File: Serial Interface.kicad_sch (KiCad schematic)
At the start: 0 parts

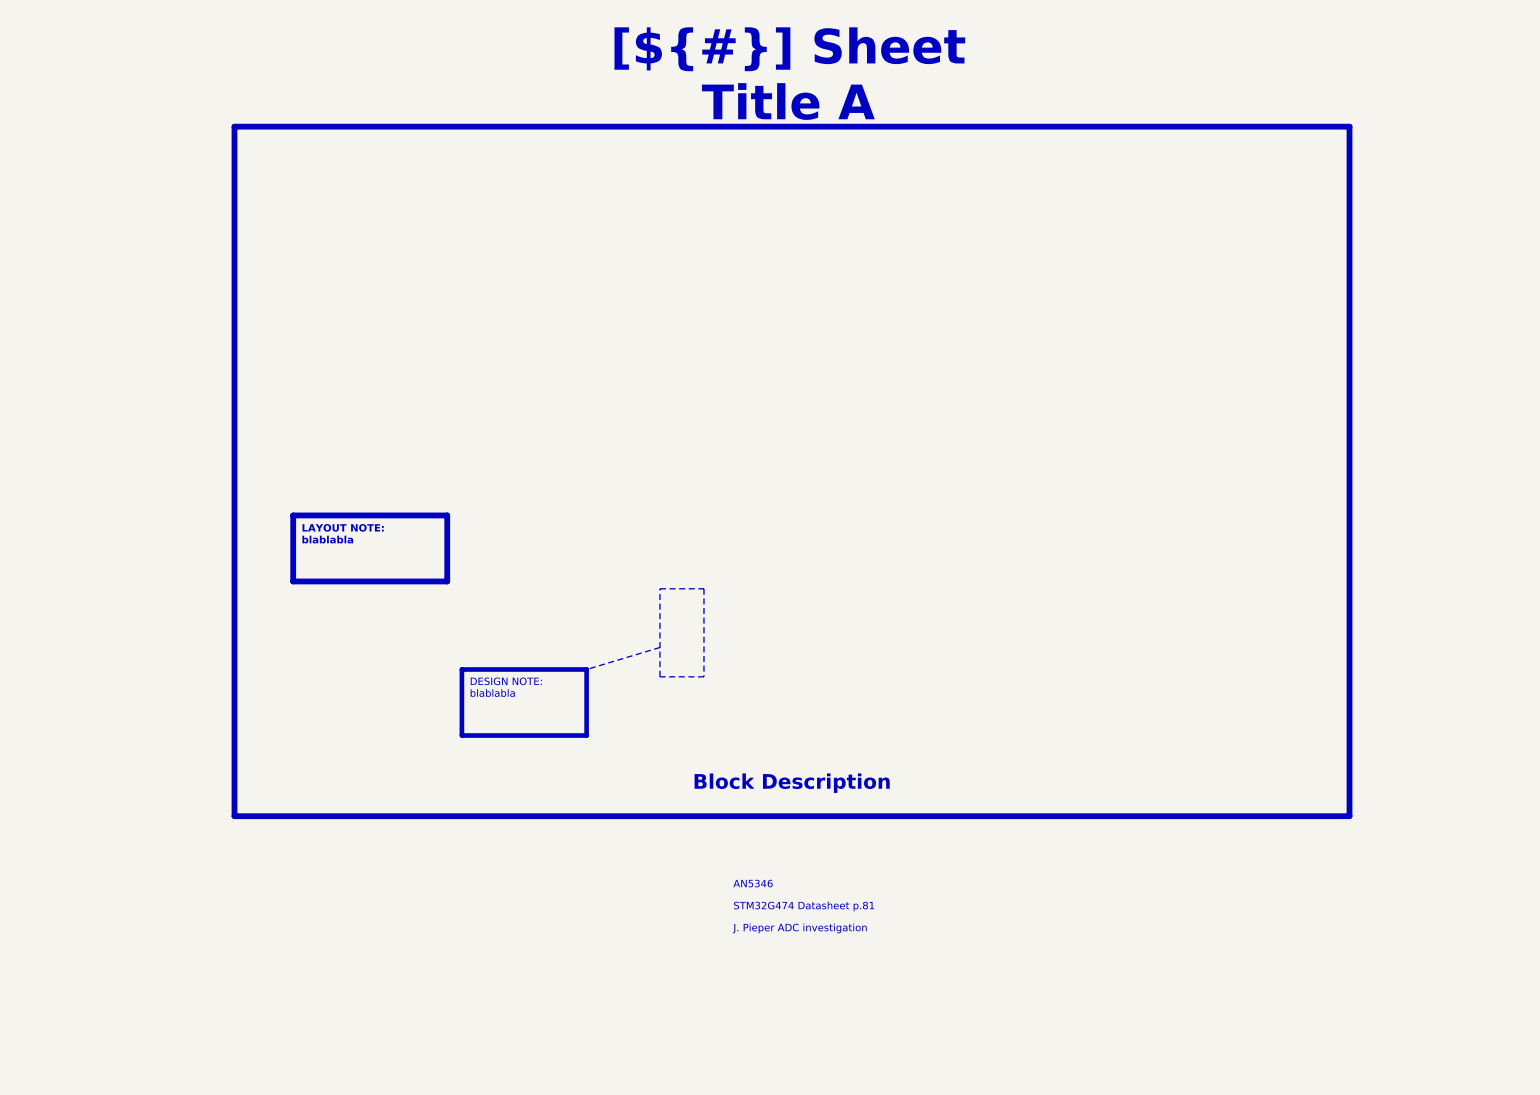
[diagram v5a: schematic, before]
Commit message: [Project][Added] CI/CD environment
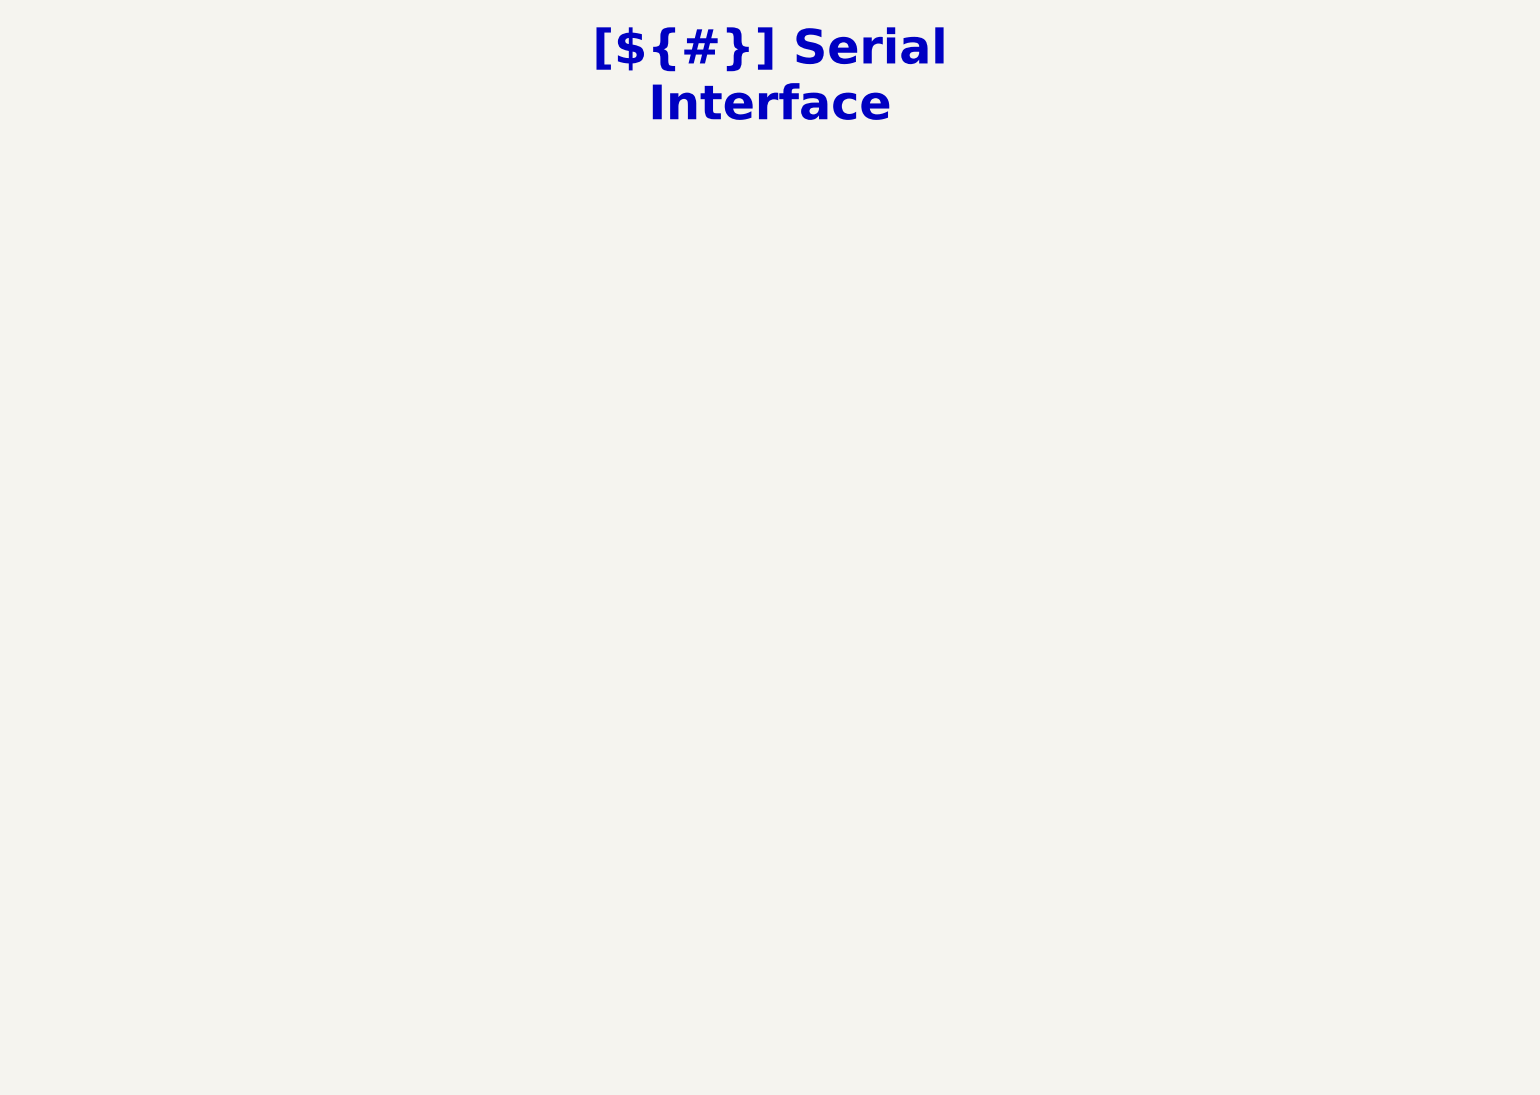
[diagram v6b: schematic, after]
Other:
- note removed: "AN5346"
- note removed: "J. Pieper ADC investigation"
- note removed: "STM32G474 Datasheet p.81"
- title: Sheet Title A -> Serial Interface
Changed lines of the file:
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@@
 (kicad_sch
-	(version 20260306)
+	(version 20250114)
 	(generator "eeschema")
-	(generator_version "10.0")
+	(generator_version "9.0")
 	(paper "A4")
 	(title_block
-		(title "Sheet Title A")
+		(title "Serial Interface")
 		(date "2025-01-12")
 		(rev "${REVISION}")
 		(company "${COMPANY}")
 	)
-	(rectangle
-		(start 129.54 110.49)
-		(end 137.16 125.73)
-		(stroke
-			(width 0)
-			(type dot)
-			(color 255 0 0 1)
-		)
-		(fill
-			(type none)
-		)
-	)
-	(rectangle
-		(start 55.88 30.48)
-		(end 248.92 149.86)
-		(stroke
-			(width 1)
-			(type default)
-			(color 200 200 200 1)
-		)
-		(fill
-			(type none)
-		)
-	)
-	(text "J. Pieper ADC investigation"
-		(exclude_from_sim no)
-		(at 142.24 170.18 0)
-		(effects
-			(font
-				(face "Arial")
-				(size 1.27 1.27)
-				(color 0 0 0 1)
-			)
-			(justify left bottom)
-			(href "https://jpieper.com/2023/07/24/stm32g4-adc-performance-part-2/")
-		)
-	)
-	(text "STM32G474 Datasheet p.81"
-		(exclude_from_sim no)
-		(at 142.24 166.37 0)
-		(effects
-			(font
-				(face "Arial")
-				(size 1.27 1.27)
-				(color 0 0 0 1)
-			)
-			(justify left bottom)
-			(href "https://www.st.com/resource/en/datasheet/stm32g474cb.pdf")
-		)
-	)
-	(text "AN5346"
-		(exclude_from_sim no)
-		(at 142.24 162.56 0)
-		(effects
-			(font
-				(face "Arial")
-				(size 1.27 1.27)
-				(color 0 0 0 1)
-			)
-			(justify left bottom)
-			(href "https://www.st.com/resource/en/application_note/an5346-stm32g4-adc-use-tips-and-recommendations-stmicroelectronics.pdf")
-		)
-	)
-	(text_box "LAYOUT NOTE:\nblablabla"
-		(exclude_from_sim no)
-		(at 66.04 97.79 0)
-		(size 26.67 11.43)
-		(margins 1.4525 1.4525 1.4525 1.4525)
-		(stroke
-			(width 1)
-			(type solid)
-			(color 0 0 255 1)
-		)
-		(fill
-			(type none)
-		)
-		(effects
-			(font
-				(face "Arial")
-				(size 1.27 1.27)
-				(thickness 0.4)
-				(bold yes)
-				(color 0 0 255 1)
-			)
-			(justify left top)
-		)
-	)
 	(text_box "[${#}] ${TITLE}"
 		(exclude_from_sim no)
-		(at 115.57 15.24 0)
-		(size 72.39 12.7)
+		(at 104.14 15.24 0)
+		(size 88.9 12.7)
 		(margins 4.4999 4.4999 4.4999 4.4999)
 		(stroke
@@
 		)
 	)
-	(text_box "Block Description"
-		(exclude_from_sim no)
-		(at 57.15 139.7 0)
-		(size 190.5 7.62)
-		(margins 1.9049 1.9049 1.9049 1.9049)
-		(stroke
-			(width -0.0001)
-			(type default)
-		)
-		(fill
-			(type none)
-		)
-		(effects
-			(font
-				(face "Times New Roman")
-				(size 2.54 2.54)
-				(thickness 0.508)
-				(bold yes)
-				(color 162 22 34 1)
-			)
-			(justify bottom)
-		)
-	)
-	(text_box "DESIGN NOTE:\nblablabla"
-		(exclude_from_sim no)
-		(at 95.25 124.46 0)
-		(size 21.59 11.43)
-		(margins 1.3525 1.3525 1.3525 1.3525)
-		(stroke
-			(width 0.8)
-			(type solid)
-			(color 250 236 0 1)
-		)
-		(fill
-			(type none)
-		)
-		(effects
-			(font
-				(face "Arial")
-				(size 1.27 1.27)
-				(color 0 0 0 1)
-			)
-			(justify left top)
-		)
-	)
-	(polyline
-		(pts
-			(xy 129.54 120.65) (xy 116.84 124.46)
-		)
-		(stroke
-			(width 0)
-			(type dot)
-			(color 255 0 0 1)
-		)
-	)

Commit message: [Schematic][Add] Serial Interface, add schematic
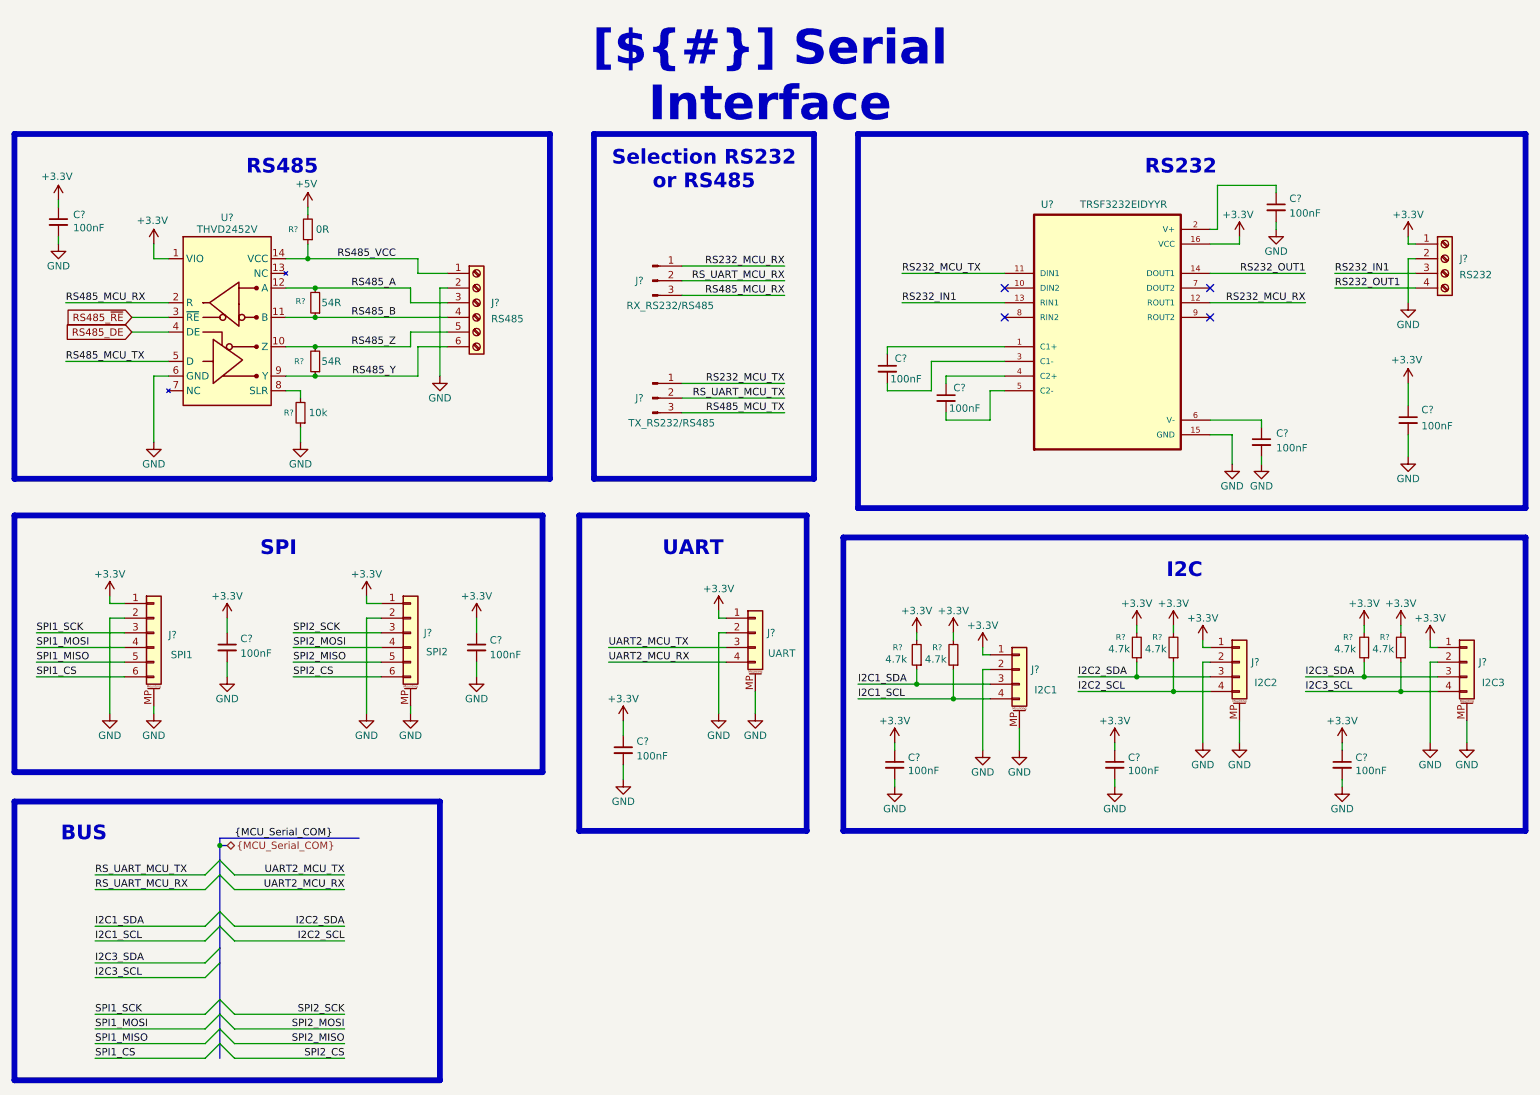
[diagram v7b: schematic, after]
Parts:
- added C? (x12): 100nF, Capacitor_SMD:C_0603_1608Metric_Pad1.08x0.95mm_HandSolder, symbol Device:C_Small
- added J? (x2): *, Connector_PinHeader_2.54mm:PinHeader_1x03_P2.54mm_Vertical, symbol Connector:Conn_01x03_Pin
- added J? (x4): *, Connector_JST:JST_PH_S4B-PH-SM4-TB_1x04-1MP_P2.00mm_Horizontal, symbol Connector_Generic_MountingPin:Conn_01x04_MountingPin
- added J? (x2): *, Connector_JST:JST_PH_S6B-PH-SM4-TB_1x06-1MP_P2.00mm_Horizontal, symbol Connector_Generic_MountingPin:Conn_01x06_MountingPin
- added J?: *, TerminalBlock_Phoenix:TerminalBlock_Phoenix_MKDS-1,5-6-5.08_1x06_P5.08mm_Horizontal, symbol Connector:Screw_Terminal_01x06
- added J?: *, TerminalBlock_Phoenix:TerminalBlock_Phoenix_MKDS-1,5-4-5.08_1x04_P5.08mm_Horizontal, symbol Connector:Screw_Terminal_01x04
- added R? (x6): 4.7k, Resistor_SMD:R_0603_1608Metric_Pad0.98x0.95mm_HandSolder, symbol Device:R_Small
- added R?: 10k, Resistor_SMD:R_0603_1608Metric_Pad0.98x0.95mm_HandSolder, symbol Device:R_Small
- added R? (x2): 54R, Resistor_SMD:R_0603_1608Metric_Pad0.98x0.95mm_HandSolder, symbol Device:R_Small
- added R?: 0R, Resistor_SMD:R_0603_1608Metric_Pad0.98x0.95mm_HandSolder, symbol Device:R_Small
- added U?: *, Package_SO:SOIC-14_3.9x8.7mm_P1.27mm, symbol P_Interface:THVD2452V
- added U?: *, Package_SO:Texas_DYY0016A_TSOT-23-16_2x4.2mm_P0.5mm, symbol P_Interface:TRSF3232EIDYYR
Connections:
- new net: C?.1, U?.1 (C1+)
- new net: C?.2, U?.3 (C1-)
- new net: R?.2, U?.8 (SLR)
- new net: C?.1, U?.2 (V+)
- new net: C?.1, U?.4 (C2+)
- new net: C?.2, U?.5 (C2-)
- new net: C?.1, U?.6 (V-)
- new net +3.3V: C?.1, C?.1, C?.1, C?.1, C?.1, C?.1, C?.1, C?.1, J?.1 (Pin_1), J?.1 (Pin_1), J?.1 (Pin_1), J?.1 (Pin_1), J?.1 (Pin_1), J?.1 (Pin_1), J?.1 (Pin_1), R?.2, R?.2, R?.2, R?.2, R?.2, R?.2, U?.1 (VIO), U?.16 (VCC)
- new net +5V: R?.2
- new net GND: C?.2, C?.2, C?.2, C?.2, C?.2, C?.2, C?.2, C?.2, C?.2, C?.2, J?.2 (Pin_2), J?.2 (Pin_2), J?.2 (Pin_2), J?.2 (Pin_2), J?.2 (Pin_2), J?.2 (Pin_2), J?.2 (Pin_2), J?.2 (Pin_2), J?.MP (MountPin), J?.MP (MountPin), J?.MP (MountPin), J?.MP (MountPin), J?.MP (MountPin), J?.MP (MountPin), R?.1, U?.15 (GND), U?.6 (GND)
- new net I2C1_SCL: J?.4 (Pin_4), R?.1
- new net I2C1_SDA: J?.3 (Pin_3), R?.1
- new net I2C2_SCL: J?.4 (Pin_4), R?.1
- new net I2C2_SDA: J?.3 (Pin_3), R?.1
- new net I2C3_SCL: J?.4 (Pin_4), R?.1
- new net I2C3_SDA: J?.3 (Pin_3), R?.1
- new net RS232_IN1: J?.3 (Pin_3), U?.13 (RIN1)
- new net RS232_MCU_RX: J?.1 (Pin_1), U?.12 (ROUT1)
- new net RS232_MCU_TX: J?.1 (Pin_1), U?.11 (DIN1)
- new net RS232_OUT1: J?.4 (Pin_4), U?.14 (DOUT1)
- new net RS485_A: J?.3 (Pin_3), R?.2, U?.12 (A)
- new net RS485_B: J?.4 (Pin_4), R?.1, U?.11 (B)
- new net RS485_DE: U?.4 (DE)
- new net RS485_MCU_RX: J?.3 (Pin_3), U?.2 (R)
- new net RS485_MCU_TX: J?.3 (Pin_3), U?.5 (D)
- new net RS485_VCC: J?.1 (Pin_1), R?.1, U?.14 (VCC)
- new net RS485_Y: J?.6 (Pin_6), R?.1, U?.9 (Y)
- new net RS485_Z: J?.5 (Pin_5), R?.2, U?.10 (Z)
- new net RS485_~{RE}: U?.3 (~{RE})
- new net RS_UART_MCU_RX: J?.2 (Pin_2)
- new net RS_UART_MCU_TX: J?.2 (Pin_2)
- new net SPI1_CS: J?.6 (Pin_6)
- new net SPI1_MISO: J?.5 (Pin_5)
- new net SPI1_MOSI: J?.4 (Pin_4)
- new net SPI1_SCK: J?.3 (Pin_3)
- new net SPI2_CS: J?.6 (Pin_6)
- new net SPI2_MISO: J?.5 (Pin_5)
- new net SPI2_MOSI: J?.4 (Pin_4)
- new net SPI2_SCK: J?.3 (Pin_3)
- new net UART2_MCU_RX: J?.4 (Pin_4)
- new net UART2_MCU_TX: J?.3 (Pin_3)
- no-connect marks 0 -> 4

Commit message: [Schematic][Modify] Annotation of all  the components
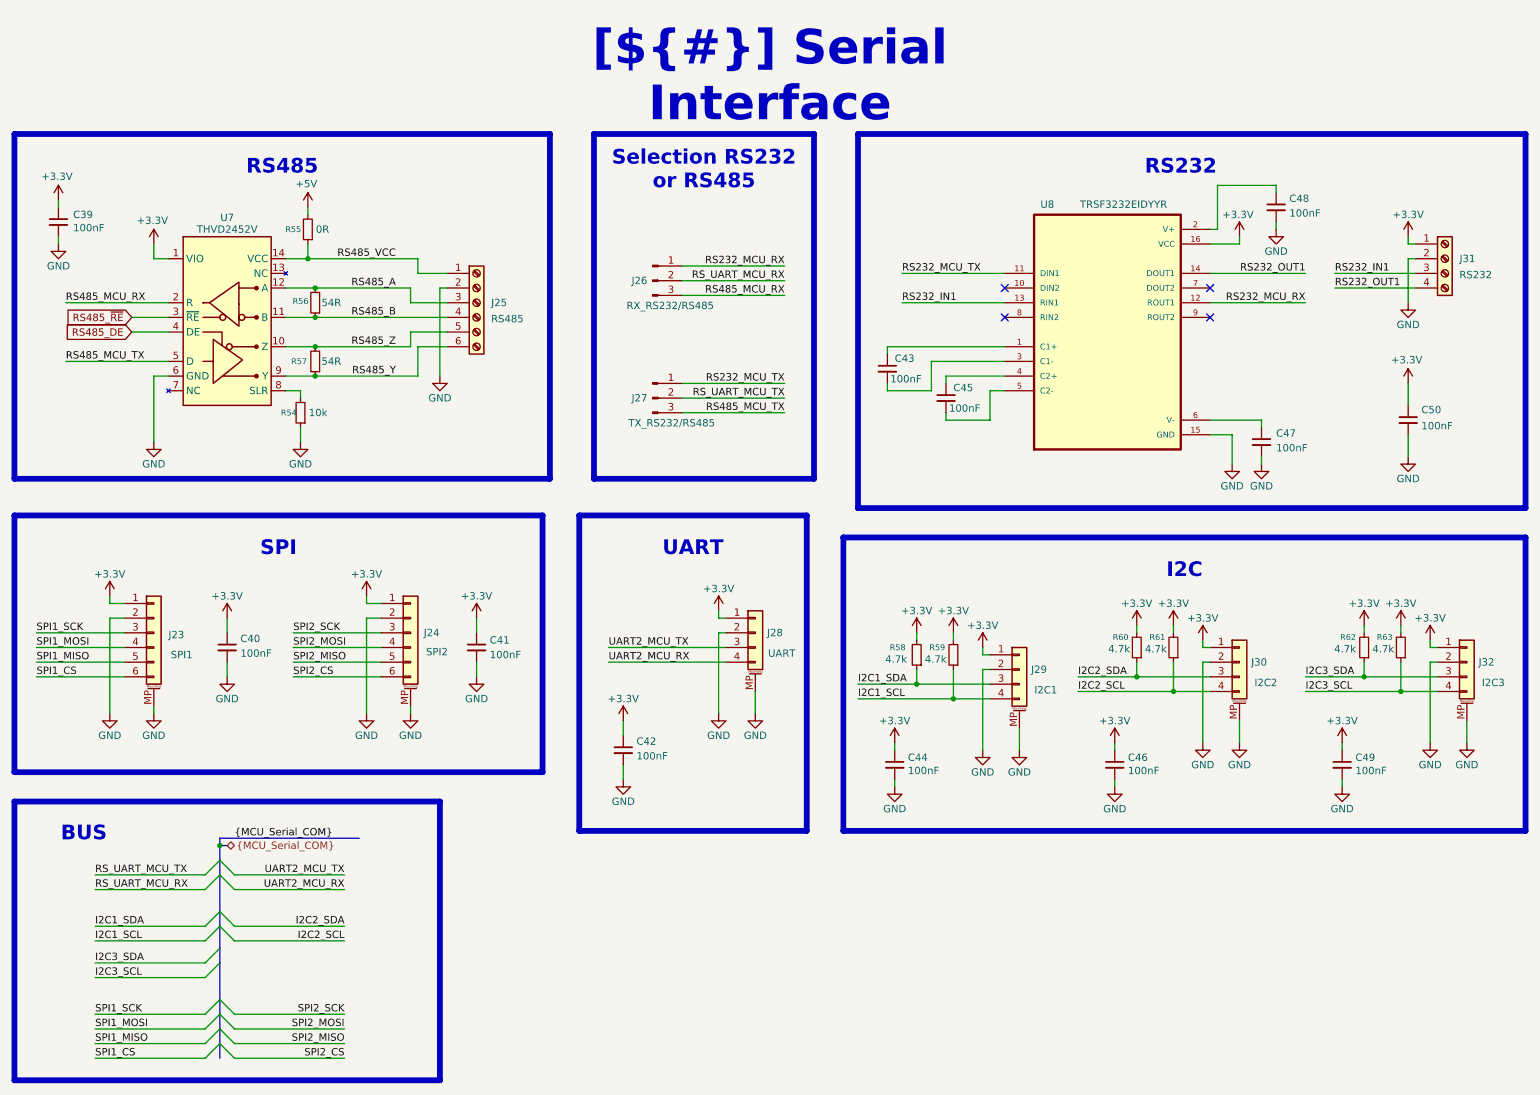
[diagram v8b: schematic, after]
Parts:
- gave numbers to parts that had none: 34
